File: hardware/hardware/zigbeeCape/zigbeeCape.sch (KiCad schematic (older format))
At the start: 31 parts

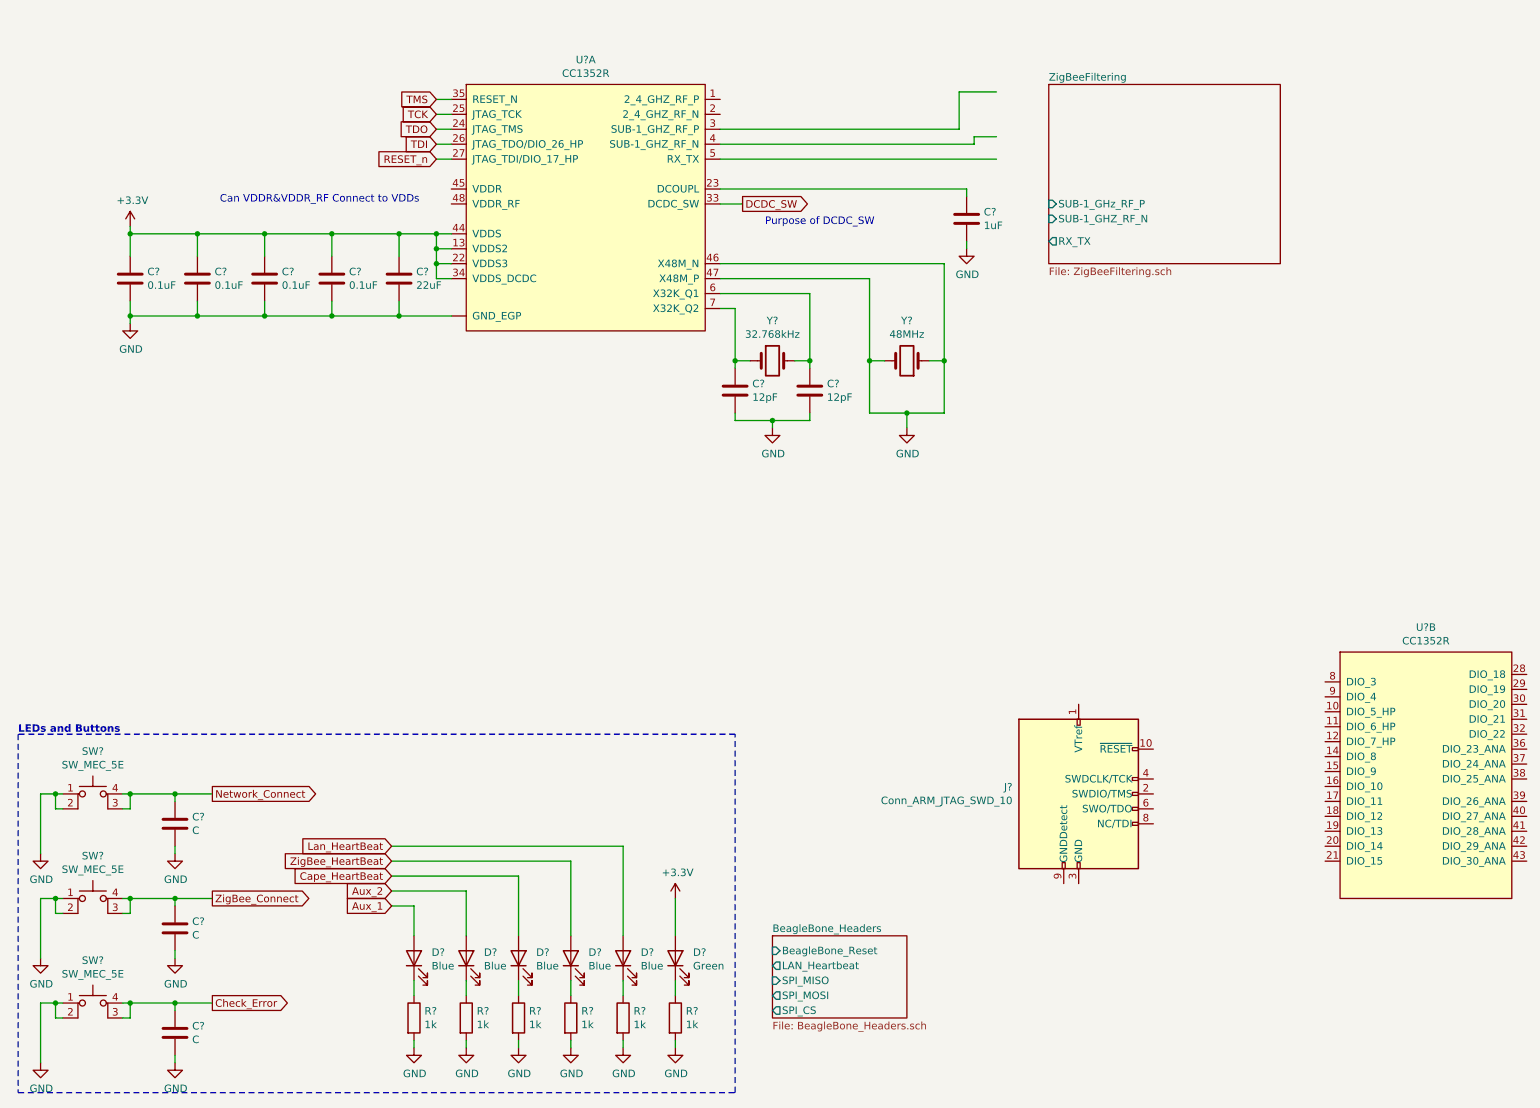
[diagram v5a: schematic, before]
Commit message: More coms lines are complete.
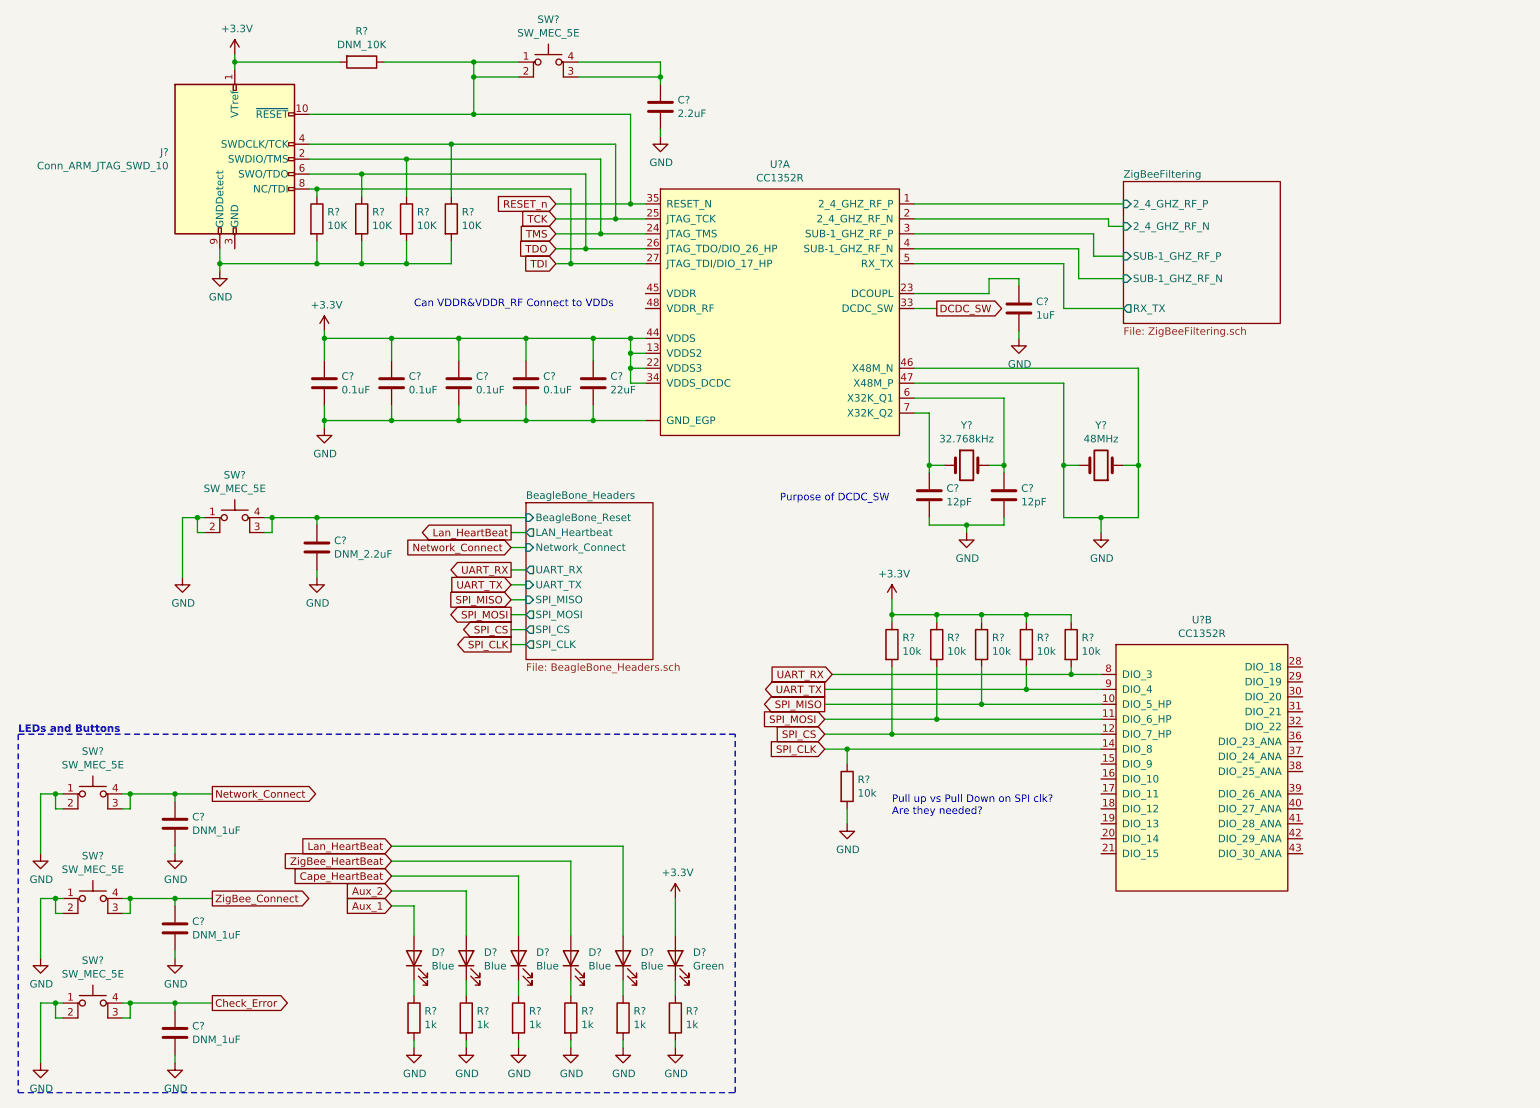
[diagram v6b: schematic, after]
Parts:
- added C?: 2.2uF, symbol Device:C
- added C?: DNM_2.2uF, symbol Device:C
- added R? (x4): 10K, symbol Device:R
- added R?: DNM_10K, symbol Device:R
- added R? (x6): 10k, symbol Device:R
- added SW? (x2): SW_MEC_5E, symbol Switch:SW_MEC_5E
- C? (x3): value C -> DNM_1uF
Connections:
- net +3V3: now also J?.1 (VTref), R?.1, R?.1, R?.1, R?.1, R?.1, R?.2
- net BeagleBone_Headers/BeagleBone_Reset: now also C?.1, SW?.3 (K), SW?.4 (A)
- net GND: now also J?.9 (GNDDetect), C?.2, C?.2, R?.2, R?.2, R?.2, R?.2, R?.2, SW?.1, SW?.2
- net RESET_n: now also J?.10 (~RESET~), U?.35 (RESET_N), R?.1, SW?.1, SW?.2; no longer U?.27 (JTAG_TDI/DIO_17_HP)
- net TCK: now also J?.4 (SWDCLK/TCK), R?.1
- net TDI: now also J?.8 (NC/TDI), U?.27 (JTAG_TDI/DIO_17_HP), R?.1; no longer U?.26 (JTAG_TDO/DIO_26_HP)
- net TDO: now also J?.6 (SWO/TDO), U?.26 (JTAG_TDO/DIO_26_HP), R?.1; no longer U?.24 (JTAG_TMS)
- net TMS: now also J?.2 (SWDIO/TMS), U?.24 (JTAG_TMS), R?.1; no longer U?.35 (RESET_N)
- net ZigBeeFiltering/RX_TX: now also U?.5 (RX_TX)
- net ZigBeeFiltering/SUB-1_GHZ_RF_N: now also U?.4 (SUB-1_GHZ_RF_N)
- net SPI_MISO: now reaches U?.10 (DIO_5_HP)
- net SPI_MISO: now also R?.2
- net SPI_MOSI: now reaches U?.11 (DIO_6_HP)
- net SPI_MOSI: now also R?.2
- net SPI_CS: now reaches U?.12 (DIO_7_HP)
- net SPI_CS: now also R?.2
- net SPI_CLK: now reaches U?.14 (DIO_8)
- net SPI_CLK: now also R?.1
- net UART_RX: now reaches U?.8 (DIO_3)
- net UART_RX: now also R?.2
- net UART_TX: now reaches U?.9 (DIO_4)
- net UART_TX: now also R?.2
- net ZigBeeFiltering/2_4_GHZ_RF_P: now reaches U?.1 (2_4_GHZ_RF_P)
- net ZigBeeFiltering/2_4_GHZ_RF_N: now reaches U?.2 (2_4_GHZ_RF_N)
- net ZigBeeFiltering/SUB-1_GHZ_RF_P: now reaches U?.3 (SUB-1_GHZ_RF_P)
- new net: C?.1, SW?.3 (K), SW?.4 (A)
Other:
- note added: "Pull up vs Pull Down on SPI clk?\nAre they needed?"
- moved on the sheet: C?, J?, U?A, U?B, Y?

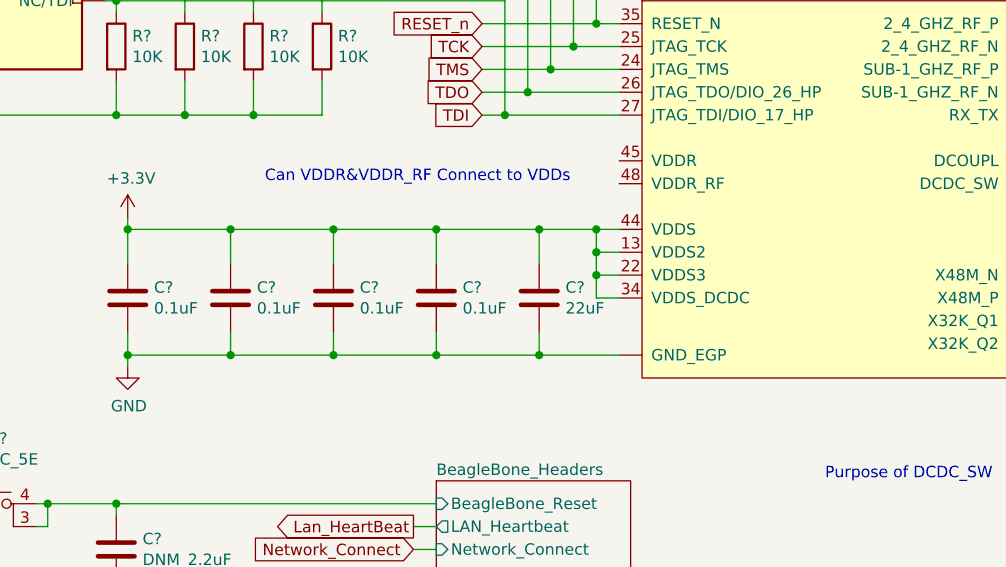
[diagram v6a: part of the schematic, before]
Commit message: Checked Parkers work on the schematic. Added commentary to indicate capacitor use for VDDS
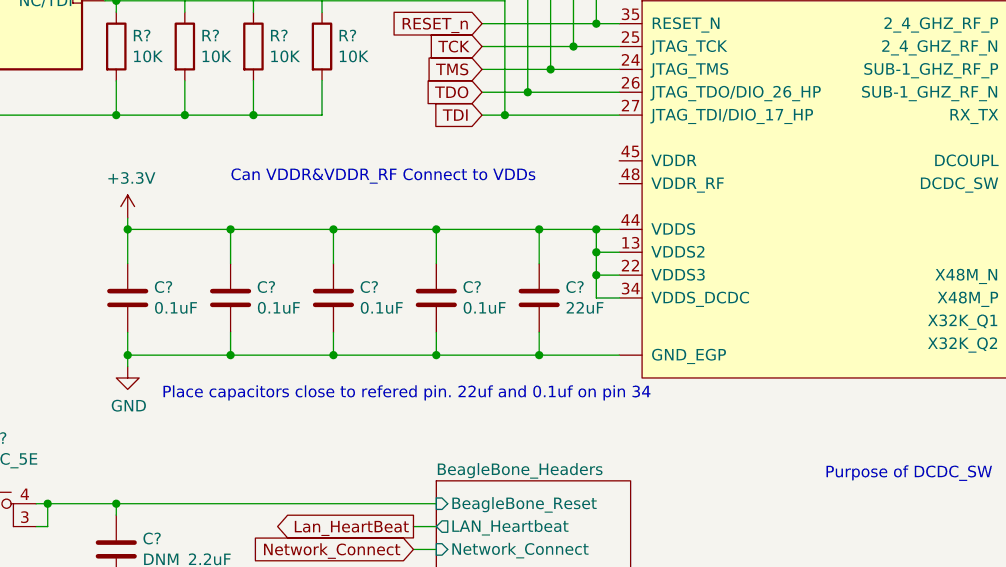
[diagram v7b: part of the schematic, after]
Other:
- note added: "Place capacitors close to refered pin. 22uf and 0.1uf on pin 34"
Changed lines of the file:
@@
 F6 "2_4_GHZ_RF_P" I L 8000 1750 50
 $EndSheet
-Text Notes 3250 2450 0    50   ~ 0
+Text Notes 3100 2450 0    50   ~ 0
 Can VDDR&VDDR_RF Connect to VDDs\n
 Text Notes 5700 3750 0    50   ~ 0
@@
 Wire Wire Line
 	6150 5800 6150 5900
+Text Notes 2800 3400 0    50   ~ 0
+Place capacitors close to refered pin. 22uf and 0.1uf on pin 34
 $EndSCHEMATC
